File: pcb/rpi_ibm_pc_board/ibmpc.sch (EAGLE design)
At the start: 31 parts, among them IC1 STM32F072C8T6, SW4 324_SW, U1 MAX3232

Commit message: clean up
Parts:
- added R10, R7, R8, R9: 2K, SparkFun-Passives:RESISTOR0805-RES
- added R3, R4: 5.1k, SparkFun-Passives:RESISTOR0805-RES
- added R5: 12K, SparkFun-Passives:RESISTOR0805-RES
- added SW1: 324_SW, 3pos_slide_switch_centered:324_SW
- added U$6: MCP4451, ps2:MCP4451
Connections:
- new net +UB: R10.2, R7.2, R8.2, R9.2, U$1.5V_1, U$1.5V_2, U$1.5V_3
- new net N$1: J4.CC1, R3.1
- new net N$12: IC1PORTA_H.PA10, JP4.3
- new net N$14: IC1PORTA_H.PA9, JP4.4
- new net N$15: IC1PORTA_H.PA13, JP4.1
- new net N$16: IC1PORTA_H.PA14, JP4.2
- new net N$17: R7.1, U$1.B1
- new net N$18: IC1RESET.BOOT0, R5.2, SW1.1, SW1.4
- new net N$19: R8.1, U$1.B2
- new net N$20: R9.1, U$1.B3
- new net N$21: R10.1, U$1.B4
- new net N$7: J4.CC2, R4.1
- new net N$8: IC1PORTA_H.PA12, J4.D+
- new net N$9: IC1PORTA_H.PA11, J4.D-
- new net SPI_CS: IC1PORTA_L.PA4, JP1.24
- new net SPI_MISO: IC1PORTA_L.PA6, JP1.21
- new net SPI_MOSI: IC1PORTA_L.PA7, JP1.19
- new net SPI_SCK: IC1PORTA_L.PA5, JP1.23
- net +3V3: now also JP4.6, SW1.2, SW1.3
- net GND: now also J4.GND, J4.SHLD, JP4.5, R3.2, R4.2, R5.1, U$1.GND_B1, U$1.GND_B2
- net N$13: now also IC1RESET.NRST
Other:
- moved on the sheet: IC1PORTA_H, IC1PORTA_L, IC1RESET, J4, JP4, R1

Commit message: working on IBM PC p board
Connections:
- new net N$22: IC1PORTB_L.PB6, JP1.5
- new net N$23: IC1PORTB_L.PB7, JP1.3
- new net N$24: IC1PORTB_H.PB12, U1.T2IN
- new net N$25: J3.8, U1.T2OUT
- new net PC_RTS: IC1PORTB_L.PB1, U1.R2OUT
- new net RTS_HV: J3.7, U1.R2IN
- new net STM32_RX: IC1PORTB_H.PB11, U1.R1OUT
- new net STM32_RX_HV: J3.3, U1.R1IN
- new net STM32_TX: IC1PORTB_H.PB10, U1.T1IN
- new net STM32_TX_HV: J3.2, U1.T1OUT
- net +3V3: now also IC1AN_POWER.VBAT, IC1AN_POWER.VDDA, IC1POWER.VDD_1, IC1POWER.VDD_2, IC1POWER.VDD_3, JP4.4; no longer JP4.6
- net GND: now also IC1AN_POWER.VSSA, IC1POWER.VSS_1, IC1POWER.VSS_2, IC1POWER.VSS_3, JP4.3; no longer JP4.5
- net N$12: now also JP4.5; no longer JP4.3
- net N$13: now also JP1.22
- net N$14: now also JP4.6; no longer JP4.4
- net N$18: now also JP1.32
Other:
- moved on the sheet: IC1AN_POWER, IC1PORTB_H, IC1PORTB_L

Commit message: ibm card done
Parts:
- removed JP11, JP2, JP3, JP9: (no value), pinhead:PINHD-1X4
- added C8: 100nF, clock:CAP0805
- added LED3: (no value), adafruit:LEDCHIP-LED0805
- added R11, R12: 2K, SparkFun-Passives:RESISTOR0805-RES
- added TP1, TP2, TP3, TP4: TPTP12R, testpad:TPTP12R
- added U$7, U$8, U$9: PINHD1X4, adafruit_changed:PINHD1X4
- JP4: device pinhead:PINHD-2X3 -> pinhead:PINHD-2X4
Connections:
- new net N$26: IC1PORTB_L.PB4, J1.1_DATA, U$7.2
- new net N$27: IC1PORTA_H.PA15, JP4.1, R11.1
- new net N$28: LED3.A, R11.2
- new net N$30: IC1PORTB_H.PB14, U$6.SDA
- new net N$31: IC1PORTB_H.PB13, U$6.SCL
- new net N$32: R12.1, U$6.HVC/A0
- new net N$33: U$1.X1, U$6.P0W
- new net N$34: U$1.X2, U$6.P1W
- new net N$35: U$1.Y1, U$6.P2W
- new net N$36: U$1.Y2, U$6.P3W
- new net N$37: IC1PORTC.PC13, JP1.36
- new net N$38: IC1PORTA_L.PA0, U$9.1
- new net N$39: IC1PORTA_L.PA1, U$9.2
- new net N$40: IC1PORTA_L.PA2, U$9.3
- new net N$41: IC1PORTA_L.PA3, U$9.4
- new net N$42: IC1PORTA_H.PA8, TP1.TP
- new net N$43: IC1PORTB_H.PB15, TP2.TP
- new net N$44: IC1PORTB_L.PB2, TP4.TP
- new net N$45: IC1PORTB_L.PB0, TP3.TP
- net +3V3: now also C8.2, JP4.6, U$6.VDD; no longer JP11.1, JP11.2, JP11.3, JP11.4, JP4.4, LED1.A
- net +UB: now also U$6.P0A, U$6.P1A, U$6.P2A, U$6.P3A
- net GND: now also C8.1, JP4.5, LED1.C, LED3.C, R12.2, U$6.A1, U$6.VSS, U$7.4, U$8.4; no longer JP2.1, JP3.1, JP4.3, JP9.1, JP9.2, JP9.3, JP9.4
- net N$10: now also IC1PORTB_H.PB8, U$8.2; no longer JP3.3
- net N$11: now also IC1PORTB_H.PB9, U$8.3; no longer JP3.2
- net N$12: now also JP4.7; no longer JP4.5
- net N$14: now also JP4.8; no longer JP4.6
- net N$15: now also JP4.3; no longer JP4.1
- net N$16: now also JP4.4; no longer JP4.2
- net N$17: now also IC1PORTC.PC14
- net N$19: now also IC1PORTF/OSC.PF0/OSC<=
- net N$2: now also LED1.A; no longer LED1.C
- net N$20: now also IC1PORTC.PC15
- net N$21: now also IC1PORTF/OSC.PF1/OSC=>
- net N$3: now also U$7.1; no longer JP2.4
- net N$4: now also U$8.1; no longer JP3.4
- net N$5: now also IC1PORTB_L.PB5, U$7.3; no longer JP2.2
- net N$6: now also IC1PORTB_L.PB3, JP4.2, R2.1; no longer J1.1_DATA, JP2.3
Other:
- moved on the sheet: IC1PORTC, IC1PORTF/OSC, J1, J2, LED1, R10, R2, R7, R8, R9

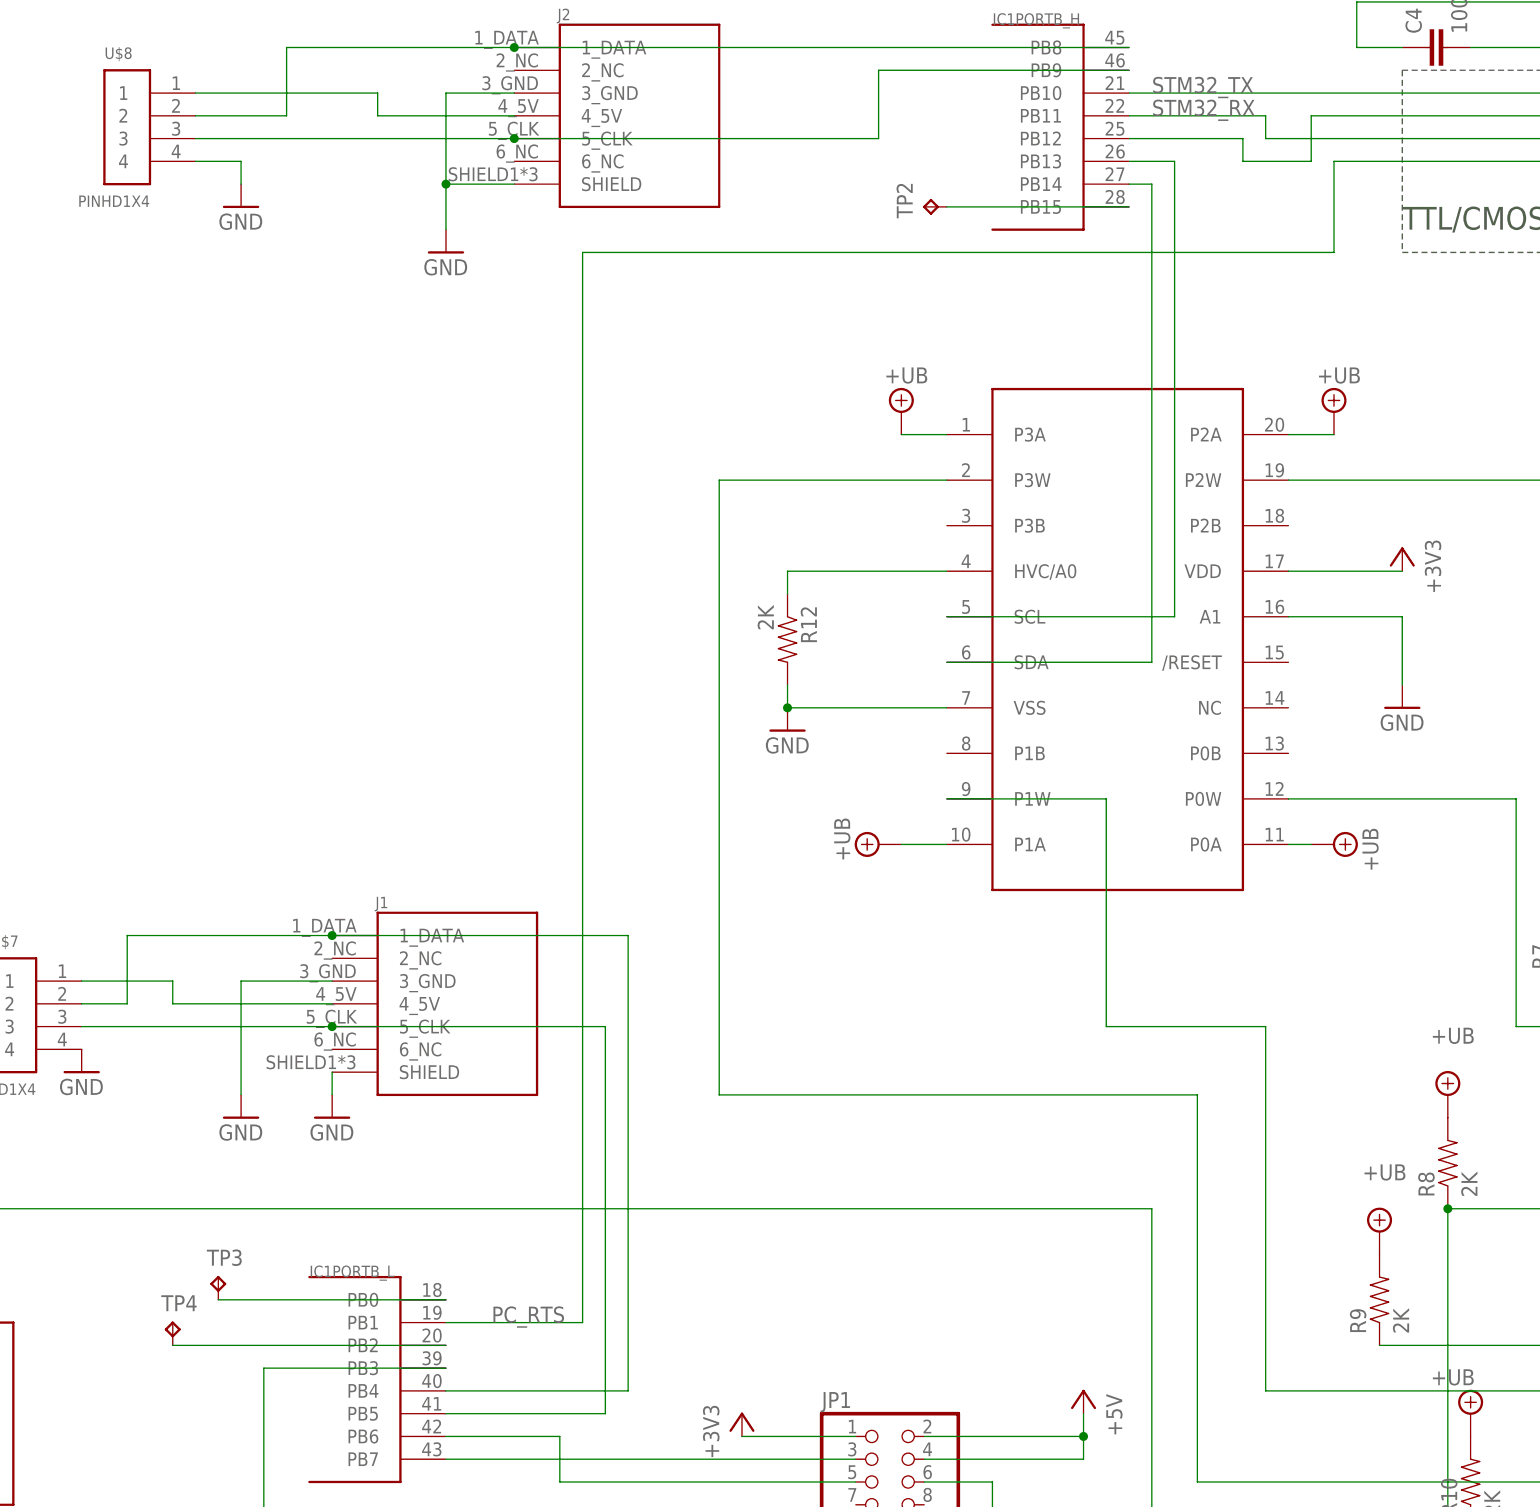
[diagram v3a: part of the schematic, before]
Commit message: added i2c pullups, cleanup
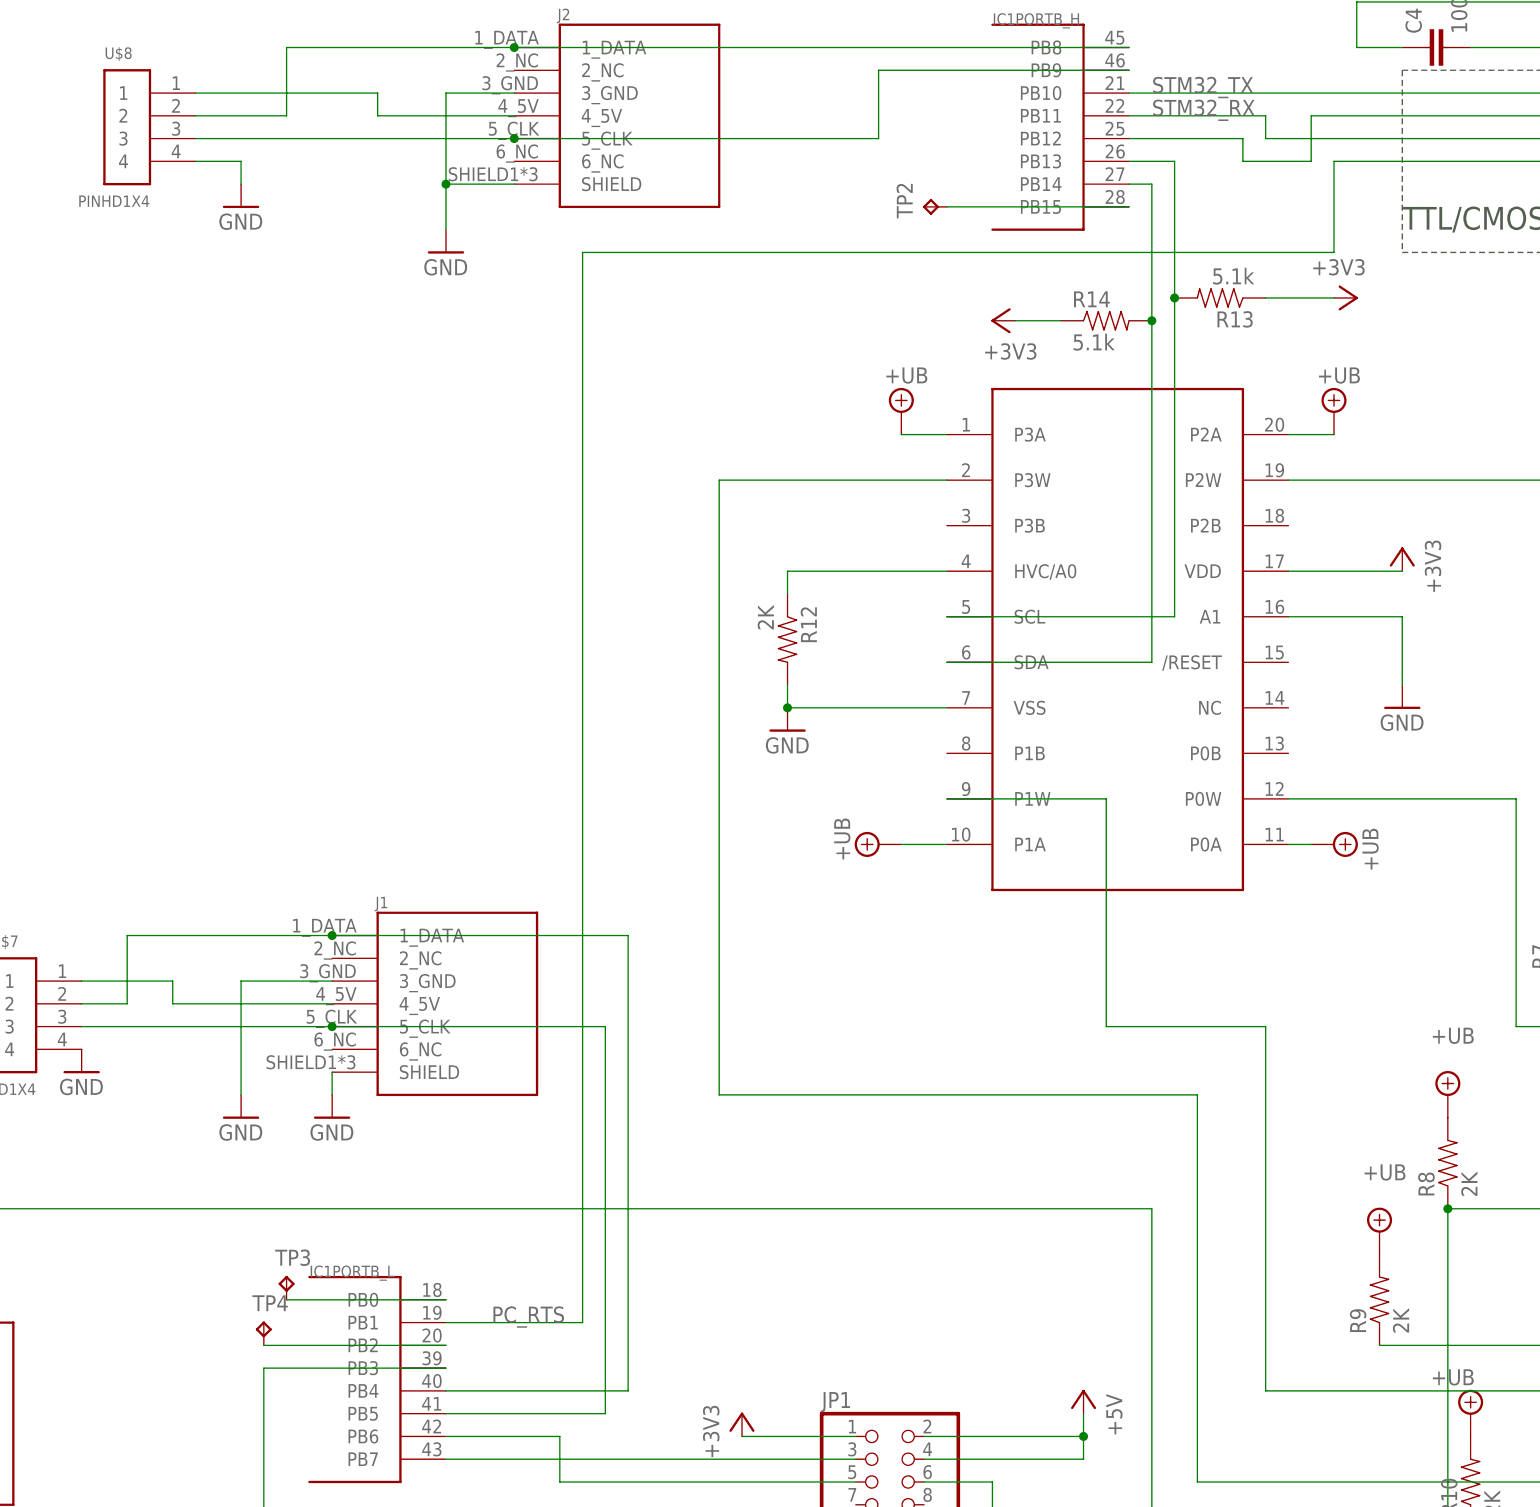
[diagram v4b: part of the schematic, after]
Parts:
- added R13, R14: 5.1k, SparkFun-Passives:RESISTOR0805-RES
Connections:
- net +3V3: now also R13.1, R14.1
- net N$30: now also R14.2
- net N$31: now also R13.2
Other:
- moved on the sheet: TP3, TP4
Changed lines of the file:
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@@
 <part name="TP3" library="testpad" library_urn="urn:adsk.eagle:library:385" deviceset="TP" device="TP12R" package3d_urn="urn:adsk.eagle:package:27963/1"/>
 <part name="TP4" library="testpad" library_urn="urn:adsk.eagle:library:385" deviceset="TP" device="TP12R" package3d_urn="urn:adsk.eagle:package:27963/1"/>
+<part name="R13" library="SparkFun-Passives" deviceset="RESISTOR" device="0805-RES" value="5.1k"/>
+<part name="R14" library="SparkFun-Passives" deviceset="RESISTOR" device="0805-RES" value="5.1k"/>
+<part name="+3V9" library="backplane" deviceset="+3V3" device=""/>
+<part name="+3V12" library="backplane" deviceset="+3V3" device=""/>
 </parts>
 <sheets>
@@
 <attribute name="TP_SIGNAL_NAME" x="97.79" y="181.61" size="1.778" layer="97" rot="R90"/>
 </instance>
-<instance part="TP3" gate="G$1" x="17.78" y="60.96" smashed="yes">
-<attribute name="NAME" x="16.51" y="62.23" size="1.778" layer="95"/>
-<attribute name="TP_SIGNAL_NAME" x="19.05" y="59.69" size="1.778" layer="97"/>
-</instance>
-<instance part="TP4" gate="G$1" x="12.7" y="55.88" smashed="yes">
-<attribute name="NAME" x="11.43" y="57.15" size="1.778" layer="95"/>
-<attribute name="TP_SIGNAL_NAME" x="13.97" y="54.61" size="1.778" layer="97"/>
+<instance part="TP3" gate="G$1" x="25.4" y="60.96" smashed="yes">
+<attribute name="NAME" x="24.13" y="62.23" size="1.778" layer="95"/>
+<attribute name="TP_SIGNAL_NAME" x="26.67" y="59.69" size="1.778" layer="97"/>
+</instance>
+<instance part="TP4" gate="G$1" x="22.86" y="55.88" smashed="yes">
+<attribute name="NAME" x="21.59" y="57.15" size="1.778" layer="95"/>
+<attribute name="TP_SIGNAL_NAME" x="24.13" y="54.61" size="1.778" layer="97"/>
+</instance>
+<instance part="R13" gate="G$1" x="129.54" y="170.18" smashed="yes" rot="R180">
+<attribute name="NAME" x="133.35" y="168.6814" size="1.778" layer="95" rot="R180"/>
+<attribute name="VALUE" x="133.35" y="173.482" size="1.778" layer="96" rot="R180"/>
+</instance>
+<instance part="R14" gate="G$1" x="116.84" y="167.64" smashed="yes">
+<attribute name="NAME" x="113.03" y="169.1386" size="1.778" layer="95"/>
+<attribute name="VALUE" x="113.03" y="164.338" size="1.778" layer="96"/>
+</instance>
+<instance part="+3V9" gate="G$1" x="104.14" y="167.64" smashed="yes" rot="R90">
+<attribute name="VALUE" x="109.22" y="165.1" size="1.778" layer="96" rot="R180"/>
+</instance>
+<instance part="+3V12" gate="G$1" x="144.78" y="170.18" smashed="yes" rot="R270">
+<attribute name="VALUE" x="139.7" y="172.72" size="1.778" layer="96"/>
 </instance>
 </instances>
@@
 <pinref part="U$6" gate="G$1" pin="VDD"/>
 <wire x1="149.86" y1="139.7" x2="137.16" y2="139.7" width="0.1524" layer="91"/>
+</segment>
+<segment>
+<pinref part="R13" gate="G$1" pin="1"/>
+<pinref part="+3V12" gate="G$1" pin="+3V3"/>
+<wire x1="142.24" y1="170.18" x2="134.62" y2="170.18" width="0.1524" layer="91"/>
+</segment>
+<segment>
+<pinref part="R14" gate="G$1" pin="1"/>
+<pinref part="+3V9" gate="G$1" pin="+3V3"/>
+<wire x1="106.68" y1="167.64" x2="111.76" y2="167.64" width="0.1524" layer="91"/>
 </segment>
 </net>
@@
 <pinref part="IC1" gate="PORTB_H" pin="PB14"/>
 <wire x1="119.38" y1="182.88" x2="121.92" y2="182.88" width="0.1524" layer="91"/>
-<wire x1="121.92" y1="182.88" x2="121.92" y2="129.54" width="0.1524" layer="91"/>
+<wire x1="121.92" y1="182.88" x2="121.92" y2="167.64" width="0.1524" layer="91"/>
 <pinref part="U$6" gate="G$1" pin="SDA"/>
+<wire x1="121.92" y1="167.64" x2="121.92" y2="129.54" width="0.1524" layer="91"/>
 <wire x1="121.92" y1="129.54" x2="99.06" y2="129.54" width="0.1524" layer="91"/>
+<pinref part="R14" gate="G$1" pin="2"/>
+<junction x="121.92" y="167.64"/>
 </segment>
 </net>
@@
 <pinref part="IC1" gate="PORTB_H" pin="PB13"/>
 <wire x1="119.38" y1="185.42" x2="124.46" y2="185.42" width="0.1524" layer="91"/>
-<wire x1="124.46" y1="185.42" x2="124.46" y2="134.62" width="0.1524" layer="91"/>
+<wire x1="124.46" y1="185.42" x2="124.46" y2="170.18" width="0.1524" layer="91"/>
 <pinref part="U$6" gate="G$1" pin="SCL"/>
+<wire x1="124.46" y1="170.18" x2="124.46" y2="134.62" width="0.1524" layer="91"/>
 <wire x1="124.46" y1="134.62" x2="99.06" y2="134.62" width="0.1524" layer="91"/>
+<pinref part="R13" gate="G$1" pin="2"/>
+<junction x="124.46" y="170.18"/>
 </segment>
 </net>
@@
 <pinref part="IC1" gate="PORTB_L" pin="PB2"/>
 <pinref part="TP4" gate="G$1" pin="TP"/>
-<wire x1="43.18" y1="53.34" x2="12.7" y2="53.34" width="0.1524" layer="91"/>
+<wire x1="43.18" y1="53.34" x2="22.86" y2="53.34" width="0.1524" layer="91"/>
 </segment>
 </net>
@@
 <pinref part="TP3" gate="G$1" pin="TP"/>
 <pinref part="IC1" gate="PORTB_L" pin="PB0"/>
-<wire x1="17.78" y1="58.42" x2="43.18" y2="58.42" width="0.1524" layer="91"/>
-</segment>
-</net>
+<wire x1="25.4" y1="58.42" x2="43.18" y2="58.42" width="0.1524" layer="91"/>
+</segment>
+</net>
